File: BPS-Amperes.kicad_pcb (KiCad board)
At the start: 2 copper layers, 40 x 50 mm, 35 parts, among them J1 Conn_02x10_Odd_Even, J2 ShuntConn, J3 PassthroughConn, J4 TestConn, J5 Conn_01x02, U1 INA186A3IDDFT, U2 OPA2196, U4 REF1930AIDDCT

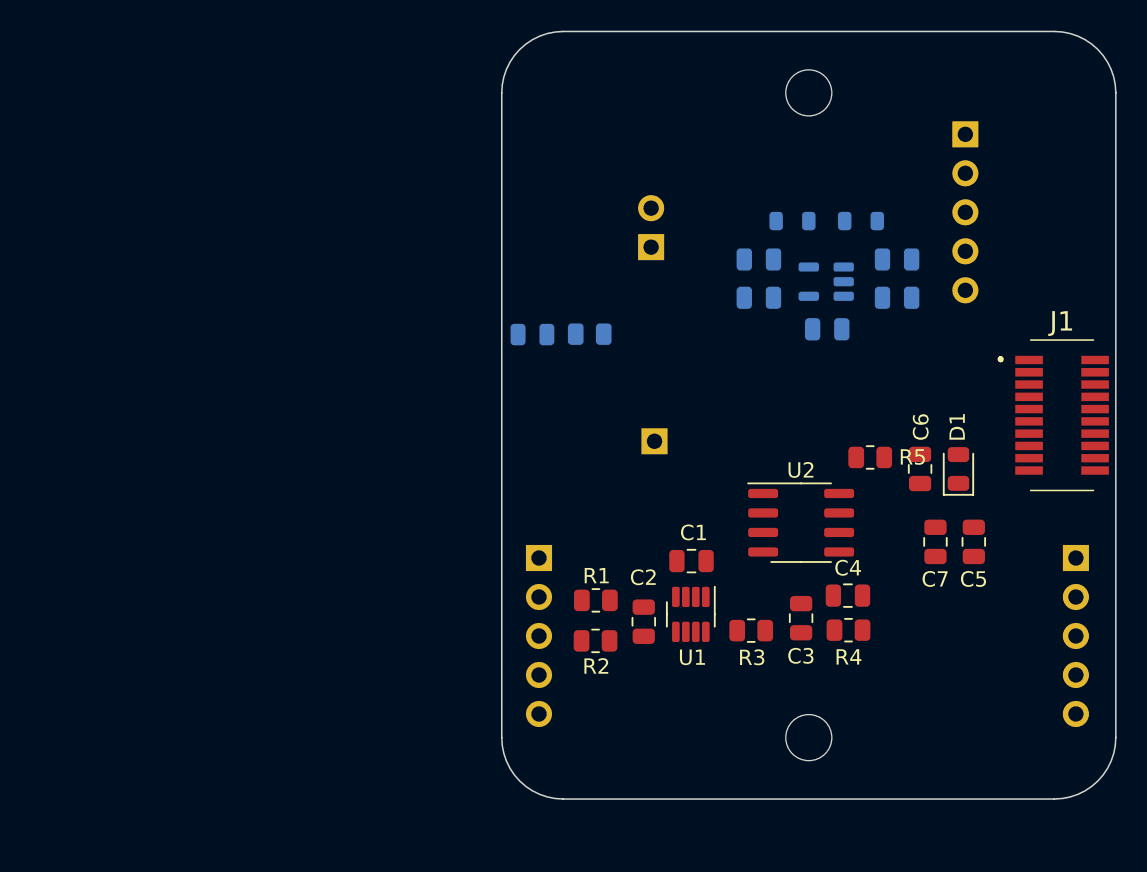
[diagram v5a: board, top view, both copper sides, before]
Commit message: Rearranged power components
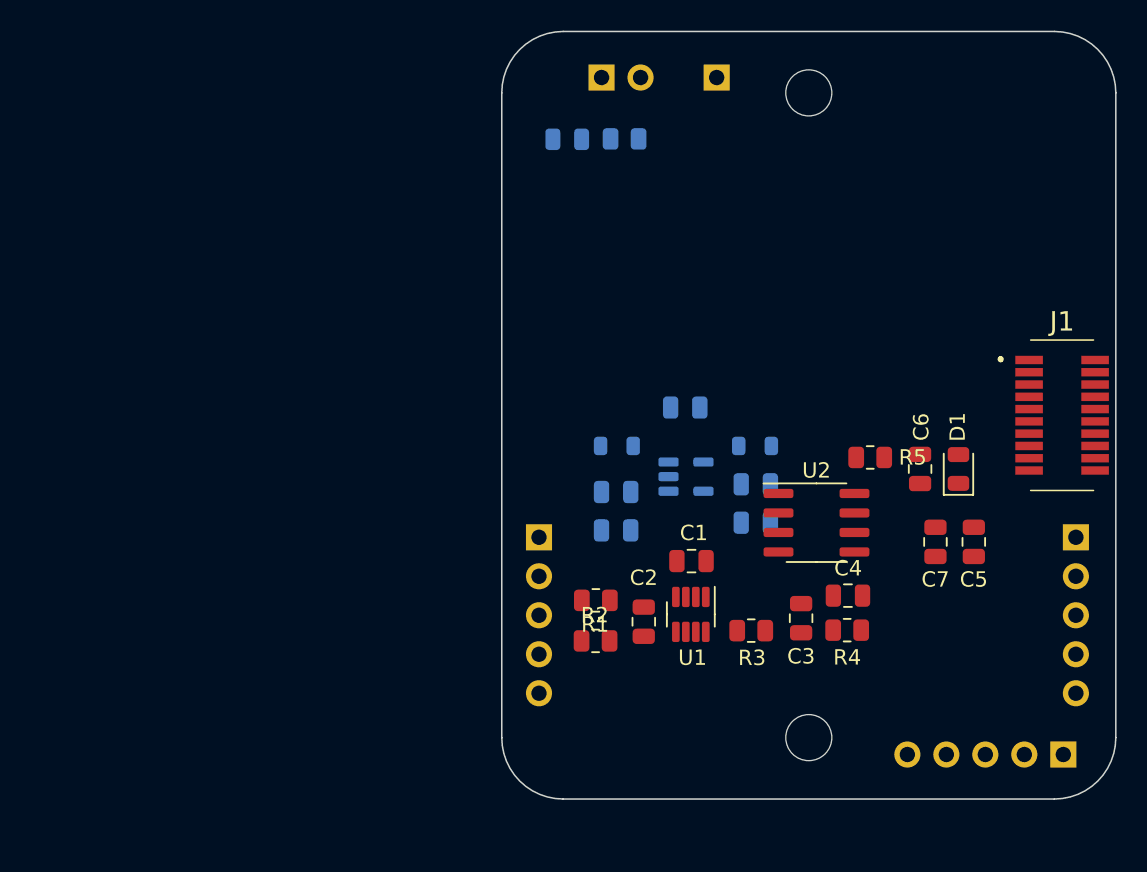
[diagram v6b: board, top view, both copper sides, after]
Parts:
- moved J4 40.9 mm to (166.6, 113.1), turned to 90 degrees
- moved C10 25.4 mm to (137.4, 98.5), turned to 180 degrees
- moved TP1 24.0 mm to (144.0, 69.0), turned to -90 degrees
- moved C9 22.2 mm to (137.4, 96.0), turned to 180 degrees
- moved FB1 21.6 mm to (137.5, 93.0), turned to 180 degrees
- moved C11 17.2 mm to (146.6, 98.0), turned to 0 degrees
- moved U4 15.6 mm to (142.0, 95.0), turned to 0 degrees
- moved FB2 14.9 mm to (146.5, 93.0), turned to 0 degrees
- moved D2 12.9 mm to (134.3, 73.0)
- moved R6 12.9 mm to (138.0, 73.0)
- moved C12 12.2 mm to (146.6, 95.5), turned to 0 degrees
- moved J5 11.5 mm to (136.5, 69.0), turned to -90 degrees
- moved C13 10.6 mm to (141.9, 90.5), turned to 180 degrees
- moved J2 1.35 mm to (132.4, 99.0)
- moved J3 1.35 mm to (167.4, 99.0)
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
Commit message: Moved power components to the front and increased spacing between components
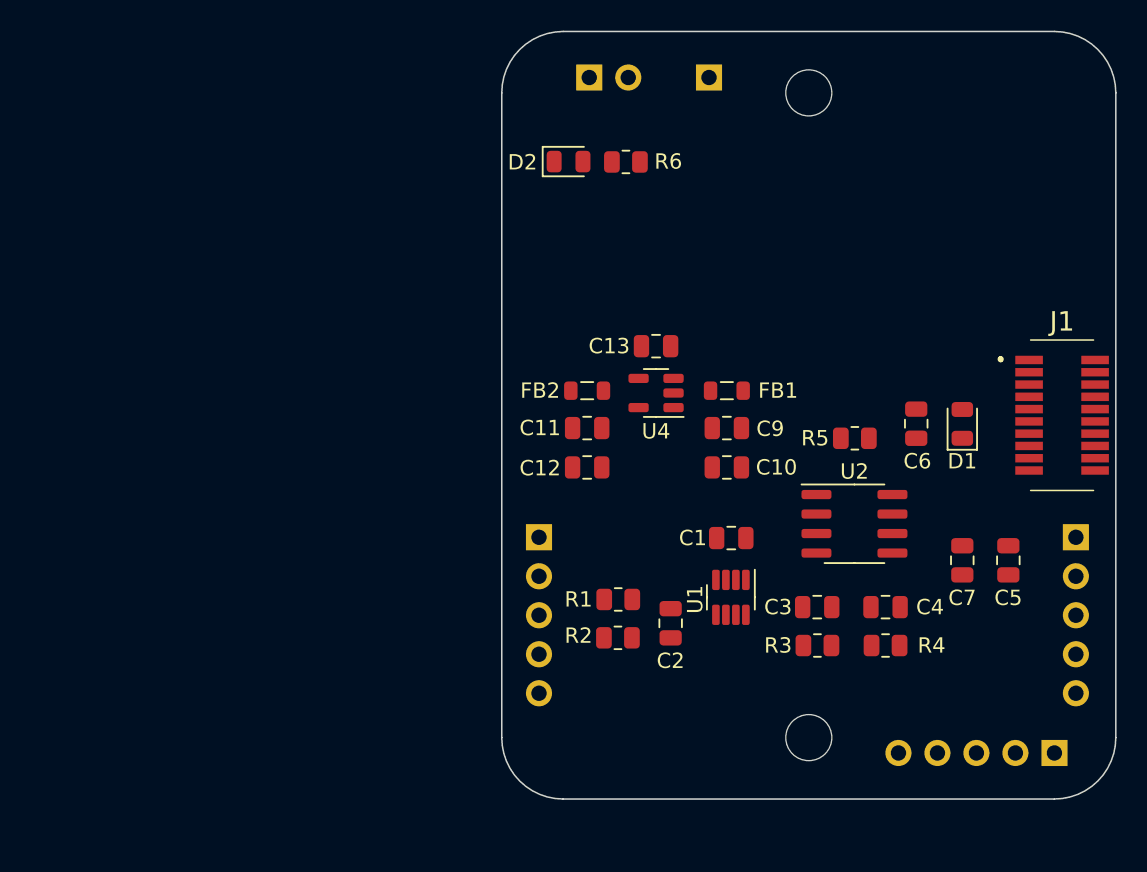
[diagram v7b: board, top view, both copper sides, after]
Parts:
- C10, C11, C12, C13, C9, D2, FB1, FB2, R6, U4: moved to F.Cu
- TP1: value Ain_TP -> Aout
- moved C11 12.6 mm to (135.6, 91.8), turned to 180 degrees
- moved FB2 11.5 mm to (135.6, 89.4), turned to 180 degrees
- moved C12 11.0 mm to (135.6, 94.4), turned to 180 degrees
- moved C9 8.33 mm to (144.7, 91.8), turned to 0 degrees
- moved C10 8.30 mm to (144.7, 94.4), turned to 0 degrees
- moved FB1 8.02 mm to (144.7, 89.4), turned to 0 degrees
- moved U4 5.79 mm to (140.1, 89.5), turned to 180 degrees
- moved C13 4.43 mm to (140.1, 86.5)
- moved R3 4.42 mm to (150.6, 106.0), turned to 180 degrees
- moved C1 2.99 mm to (144.9, 99.0)
- moved C6 2.96 mm to (157.0, 91.5)
- moved D1 2.95 mm to (160.0, 91.6)
- moved U1 2.84 mm to (144.9, 102.9)
- moved R4 2.69 mm to (155.0, 106.0)
- moved C4 2.56 mm to (155.0, 103.5)
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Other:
- board text added: "1.5V"
- board text added: "3.0V"
- board text added: "Aout"

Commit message: Changed position of headers and labelled stuff
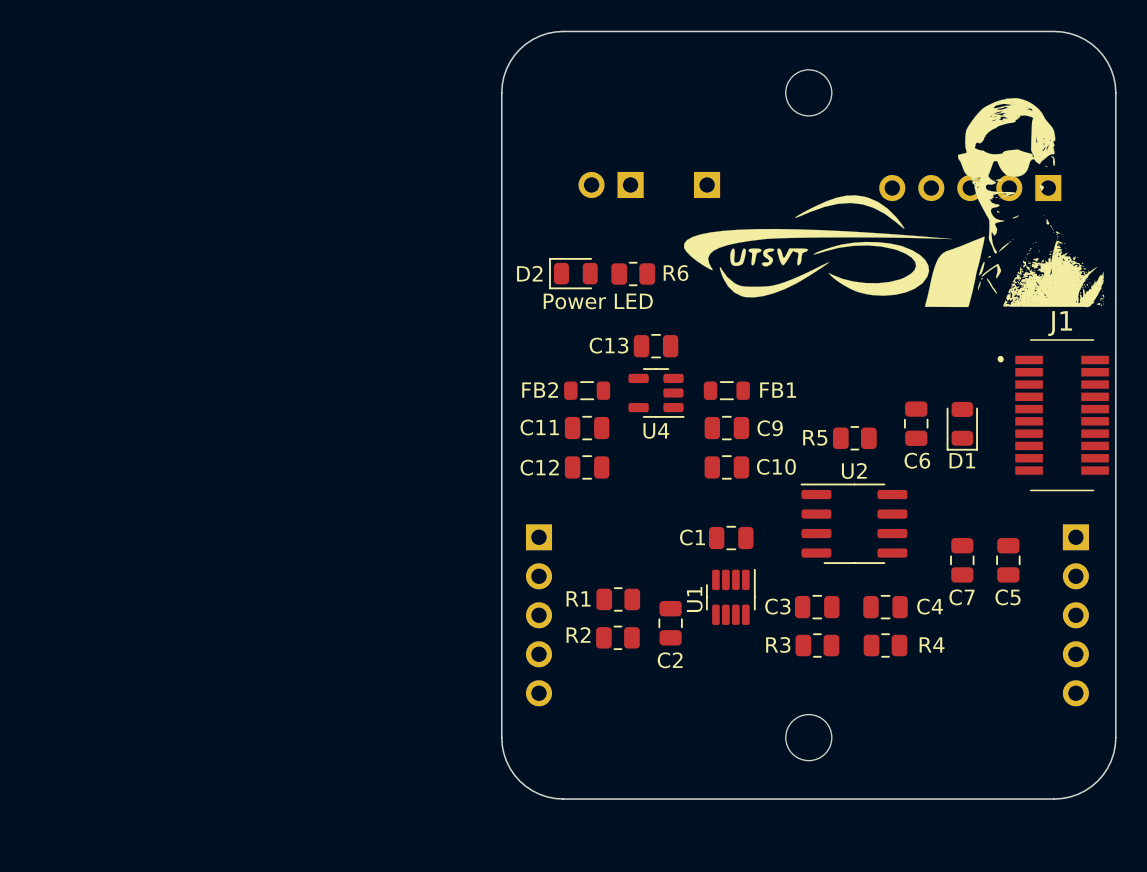
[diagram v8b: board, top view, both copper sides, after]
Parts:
- J4: footprint Connector_PinSocket_2.54mm:PinSocket_1x05_P2.54mm_Horizontal -> Connector_PinHeader_2.54mm:PinHeader_1x05_P2.54mm_Horizontal
- J5: footprint Connector_PinSocket_2.54mm:PinSocket_1x02_P2.54mm_Horizontal -> Connector_PinHeader_2.54mm:PinHeader_1x02_P2.54mm_Horizontal
- LOGO0, LOGO1: moved to F.Cu
- TP1: value Aout -> Ain_TP; footprint Connector_PinSocket_2.54mm:PinSocket_1x01_P2.54mm_Horizontal -> Connector_PinHeader_2.54mm:PinHeader_1x01_P2.54mm_Horizontal
- moved LOGO0 43.6 mm to (162.9, 77.0), turned to 0 degrees
- moved J4 36.8 mm to (165.6, 76.2)
- moved LOGO1 32.2 mm to (150.3, 80.1), turned to 0 degrees
- moved J5 7.50 mm to (138.4, 76.0), turned to 90 degrees
- moved D2 7.32 mm to (134.8, 81.8)
- moved R6 7.32 mm to (138.6, 81.8)
- moved TP1 7.00 mm to (143.4, 76.0), turned to 90 degrees
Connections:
- net Net-(J3-Pin_2) renamed /SHUNT
- net Net-(J3-Pin_3) renamed /TEST
- net Net-(J3-Pin_4) renamed /V+
- net Net-(J3-Pin_5) renamed /V-
- J5 pad 1: +1V5 -> +3V0
- J5 pad 2: +3V0 -> +1V5
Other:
- board text added: "NC"
- board text added: "Power LED"
- board text added: "SHUNT"
- board text added: "TEST"
- board text added: "Test Points"
- board text added: "V+"
- board text added: "V-"
